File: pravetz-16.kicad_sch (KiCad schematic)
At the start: 2 parts, among them U1 74LS138, U2 74LS04

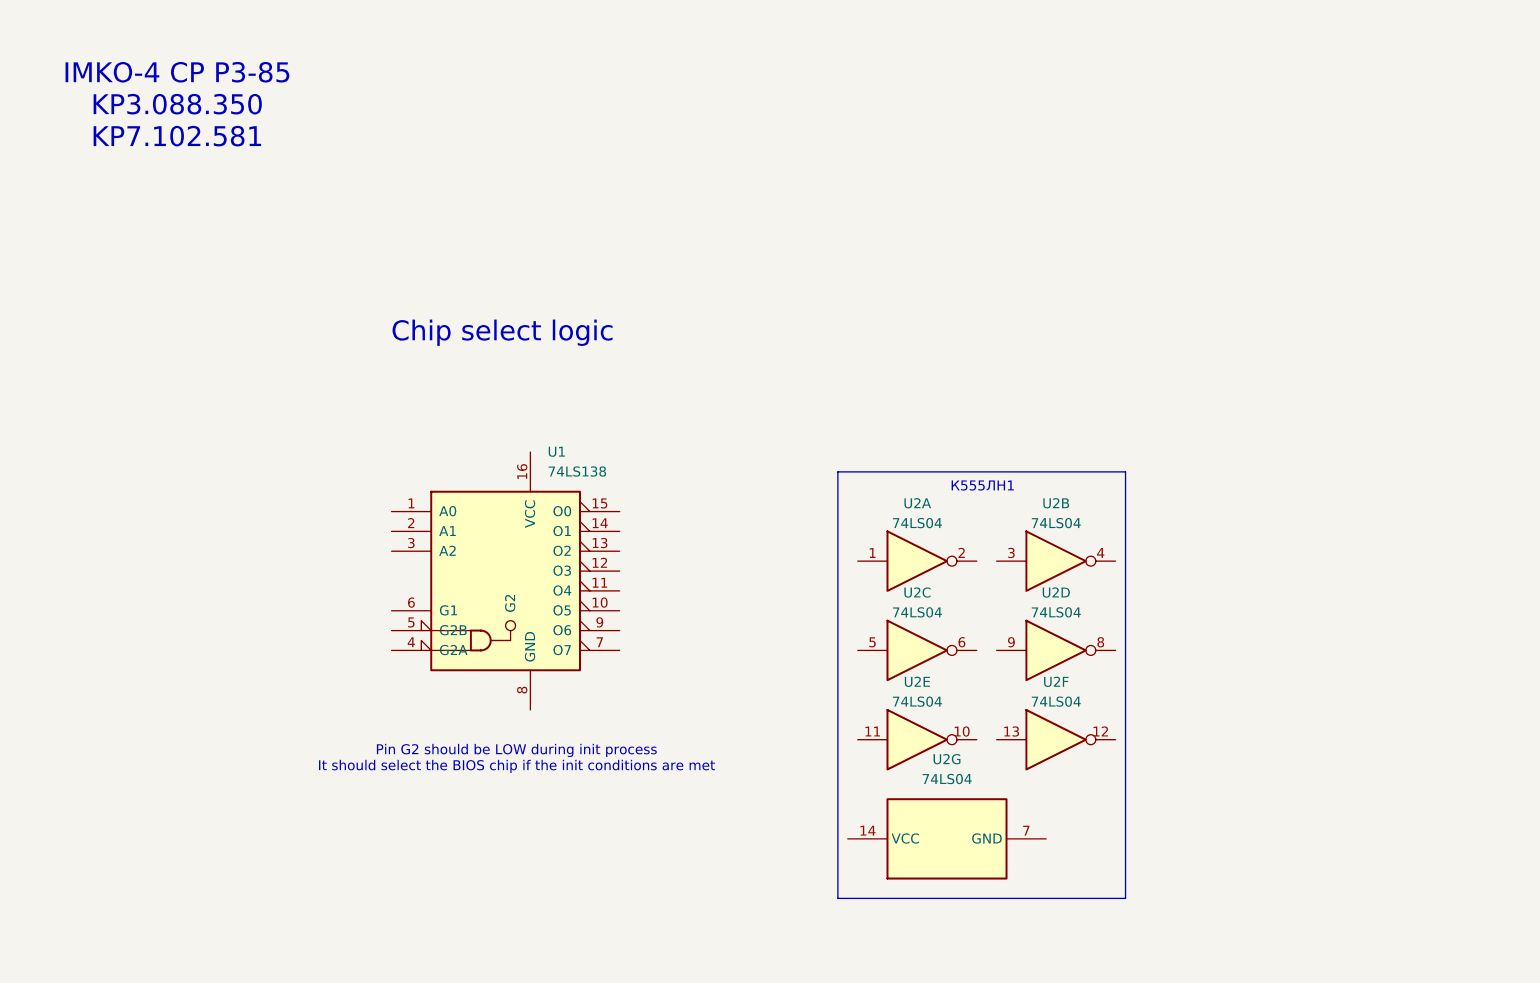
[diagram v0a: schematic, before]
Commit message: Add more chip select logic
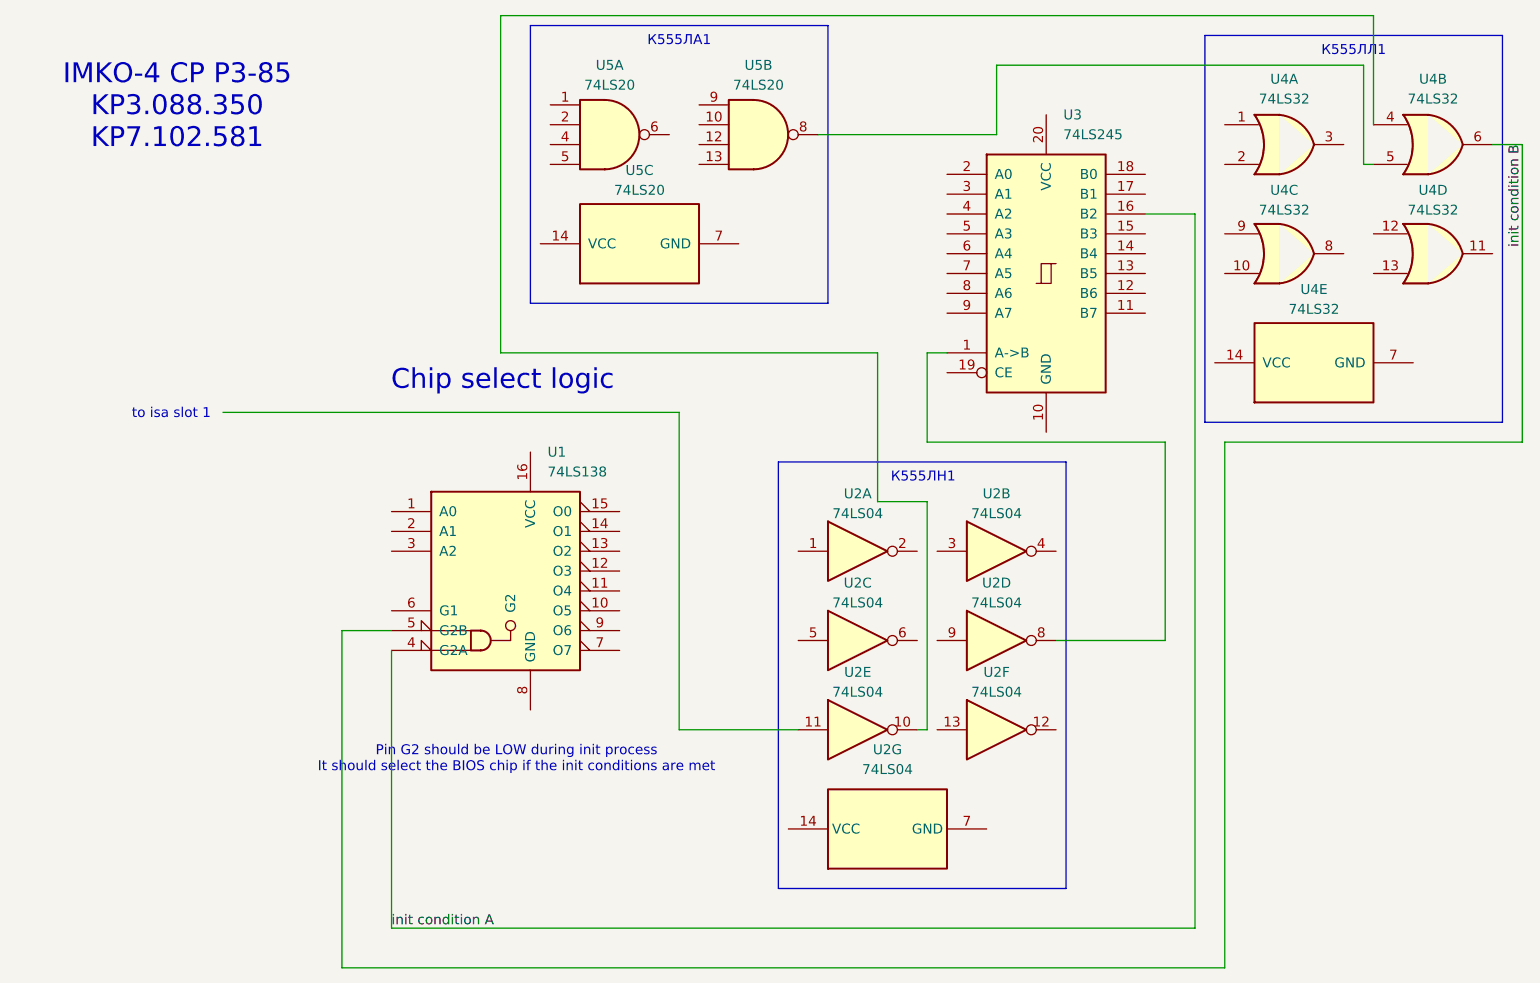
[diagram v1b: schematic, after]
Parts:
- added U3: 74LS245, symbol 74xx:74LS245
- added U4: 74LS32, symbol 74xx:74LS32
- added U5: 74LS20, symbol 74xx:74LS20
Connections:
- net at U2.8: now also U3.1 (A->B)
- net init condition A: now reaches U1.4 (G2A)
- net init condition A: now also U3.16 (B2)
- net init condition B: now reaches U1.5 (G2B)
- net init condition B: now also U4.6
- net at U2.10: now also U4.4
- new net: U4.5, U5.8
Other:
- note added: "to isa slot 1"
- note added: "К555ЛА1"
- note added: "К555ЛЛ1"
- moved on the sheet: U2A, U2B, U2C, U2D, U2E, U2F, U2G

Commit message: Add more CS logic and understand more about early init
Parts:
- added J1, J2, J3, J4, J5, J6, J7, J8: Bus_ISA_8bit, symbol Connector:Bus_ISA_8bit
- added U10, U11, U12: 74LS373, symbol 74xx:74LS373
- added U6: 74LS08, symbol 74xx:74LS08
- added U7: 74LS175, symbol 74xx:74LS175
- added U8: 74LS10, symbol 74xx:74LS10
- added U9: 74LS244, symbol 74xx:74LS244
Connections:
- net ISA SMEMR (memory read): now reaches U3.4 (A2)
- net ISA SMEMR (memory read): now also J3.12 (~{SMEMR})
- net at U2.9: now also U6.6
- net ISA OSC (1st slot): now reaches U2.11
- net ISA OSC (1st slot): now also J1.30 (OSC)
- new net: U6.4, U7.7 (Q1)
- new net D39 bus direction: U10.1 (OE), U11.1 (OE), U12.1 (OE), U6.5, U7.2 (Q0), U7.5 (D1), U8.13, U9.1 (OEa), U9.19 (OEb)
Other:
- note added: "Controls D39 bus direction"
- note added: "D12"
- note added: "D15"
- note added: "D21"
- note added: "D22"
- note added: "D27"
- note added: "D30"
- note added: "D38"
- note added: "D39"
- note added: "Data banks logic"
- note added: "TESLA MH74S10"
- note added: "К555ЛА1 D29"
- note added: "К555ЛИ1 D37"
- note added: "К555ЛЛ1 D49"
- note added: "К555ЛН1 D28"
- note removed: "to isa slot 1"
- note removed: "К555ЛА1"
- note removed: "К555ЛЛ1"
- note removed: "К555ЛН1"
- moved on the sheet: U1, U2A, U2B, U2C, U2D, U2E, U2F, U2G, U3, U4A, U4B, U4C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

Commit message: Add cpu and databanks
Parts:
- added U13: 74LS670, symbol 74xx:74LS670
- added U14: 74LS74, symbol 74xx:74LS74
- added U15: 74LS04, symbol 74xx:74LS04
- added U16: 8088, Package_DIP:DIP-40_W15.24mm, symbol MCU_Intel:8088
- added U17, U18, U19, U20, U21, U22: TMM2464AP, symbol Memory_ROM:TMM2464AP
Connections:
- net init condition A is gone; now on net !reset: U1.4 (G2A), U3.16 (B2)
- net at U12.2 (O0): now also U5.10, U13.10 (Q1), U13.11 (~{Er})
- net at U12.5 (O1): now also U5.12, U13.9 (Q2)
- net at U12.6 (O2): now also U5.13, U13.7 (Q3)
- net at U12.9 (O3): now also U5.9, U13.6 (Q4)
- net !reset: now reaches U1.6 (G1)
- net !reset: now also U14.1 (~{R}), U15.3, U15.4, U16.21 (RESET)
- net bios select: now reaches U1.7 (O7)
- net bios select: now also U17.22 (OE)
- net init condition B renamed init condition 2.B
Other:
- note added: "74LS74AN D44"
- note added: "CPU"
- note added: "D10"
- note added: "D23 BIOS"
- note added: "D24"
- note added: "D25"
- note added: "D26"
- note added: "D33"
- note added: "D34"
- note added: "D42"
- note added: "К555ЛН1 D46"
- moved on the sheet: U1

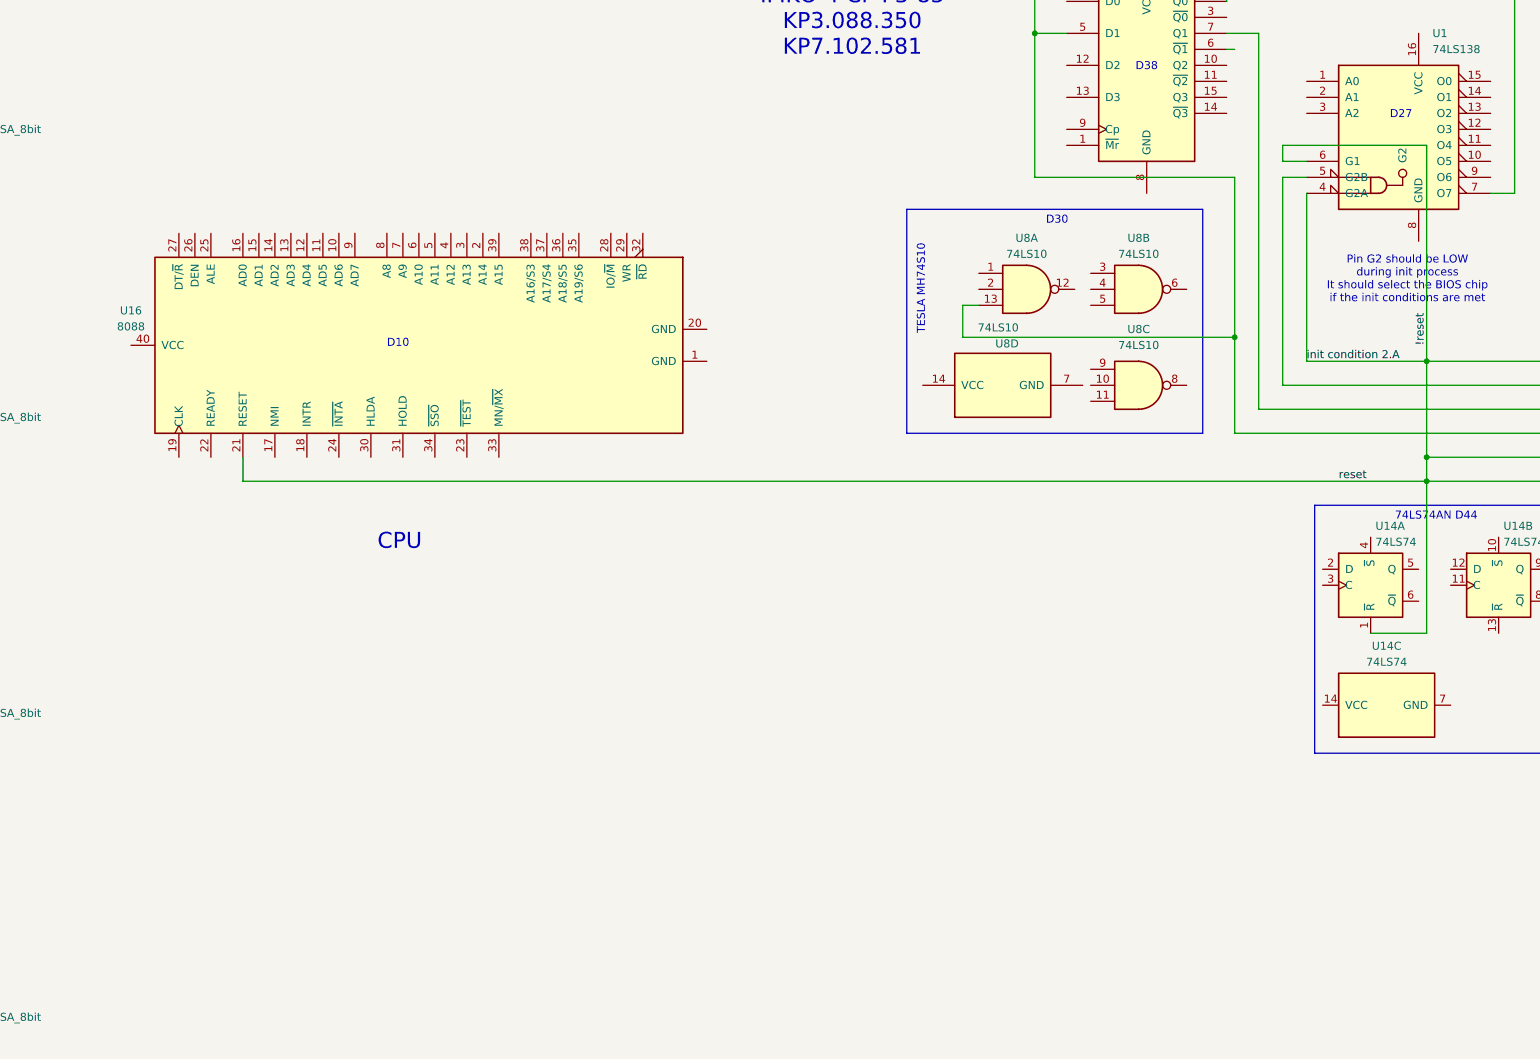
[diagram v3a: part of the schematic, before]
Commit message: Add 8259 chip
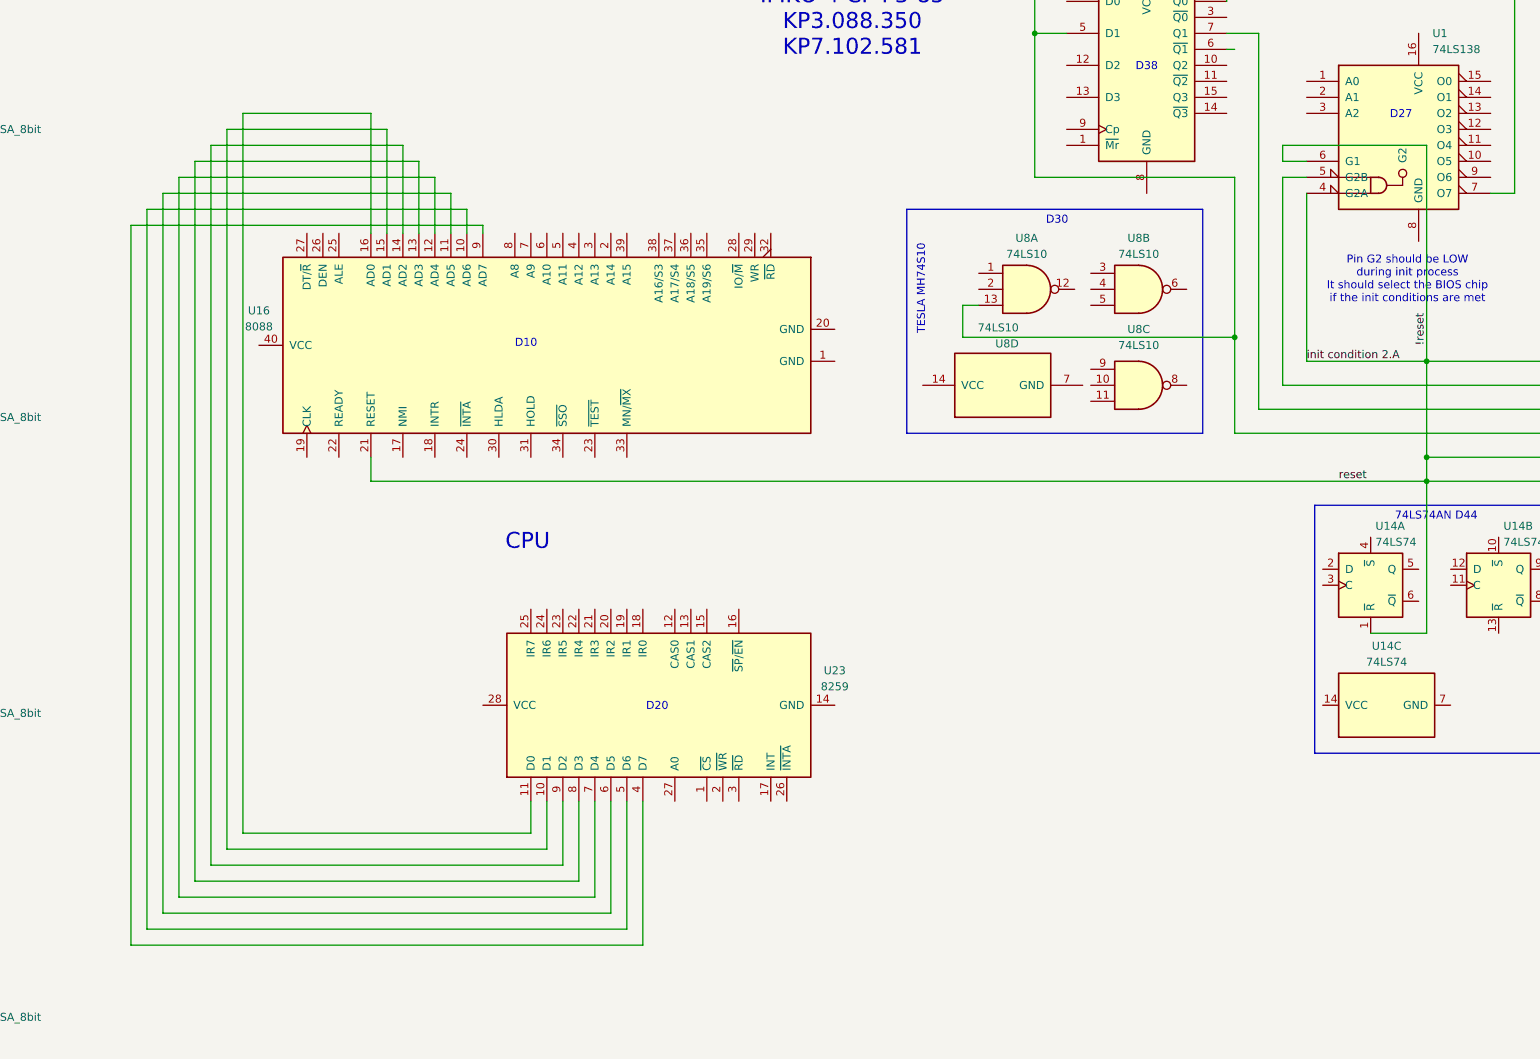
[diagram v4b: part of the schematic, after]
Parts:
- added U23: 8259, Package_DIP:DIP-28_W15.24mm, symbol Interface:8259
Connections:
- net at U16.10 (AD6): now also U23.5 (D6)
- net at U16.11 (AD5): now also U23.6 (D5)
- net at U16.12 (AD4): now also U23.7 (D4)
- net at U16.13 (AD3): now also U23.8 (D3)
- net at U16.14 (AD2): now also U23.9 (D2)
- net at U16.15 (AD1): now also U23.10 (D1)
- net at U16.16 (AD0): now also U23.11 (D0)
- net at U16.9 (AD7): now also U23.4 (D7)
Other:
- note added: "D20"
- moved on the sheet: U16
